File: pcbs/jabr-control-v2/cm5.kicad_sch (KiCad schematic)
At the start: 22 parts, among them J201 JST-SH-4-Vertical, Q201 DMN21D2UFB-7B, SW201 TS20-42-25-WT-160-SMT-TR, U201 NX3DV221TKX

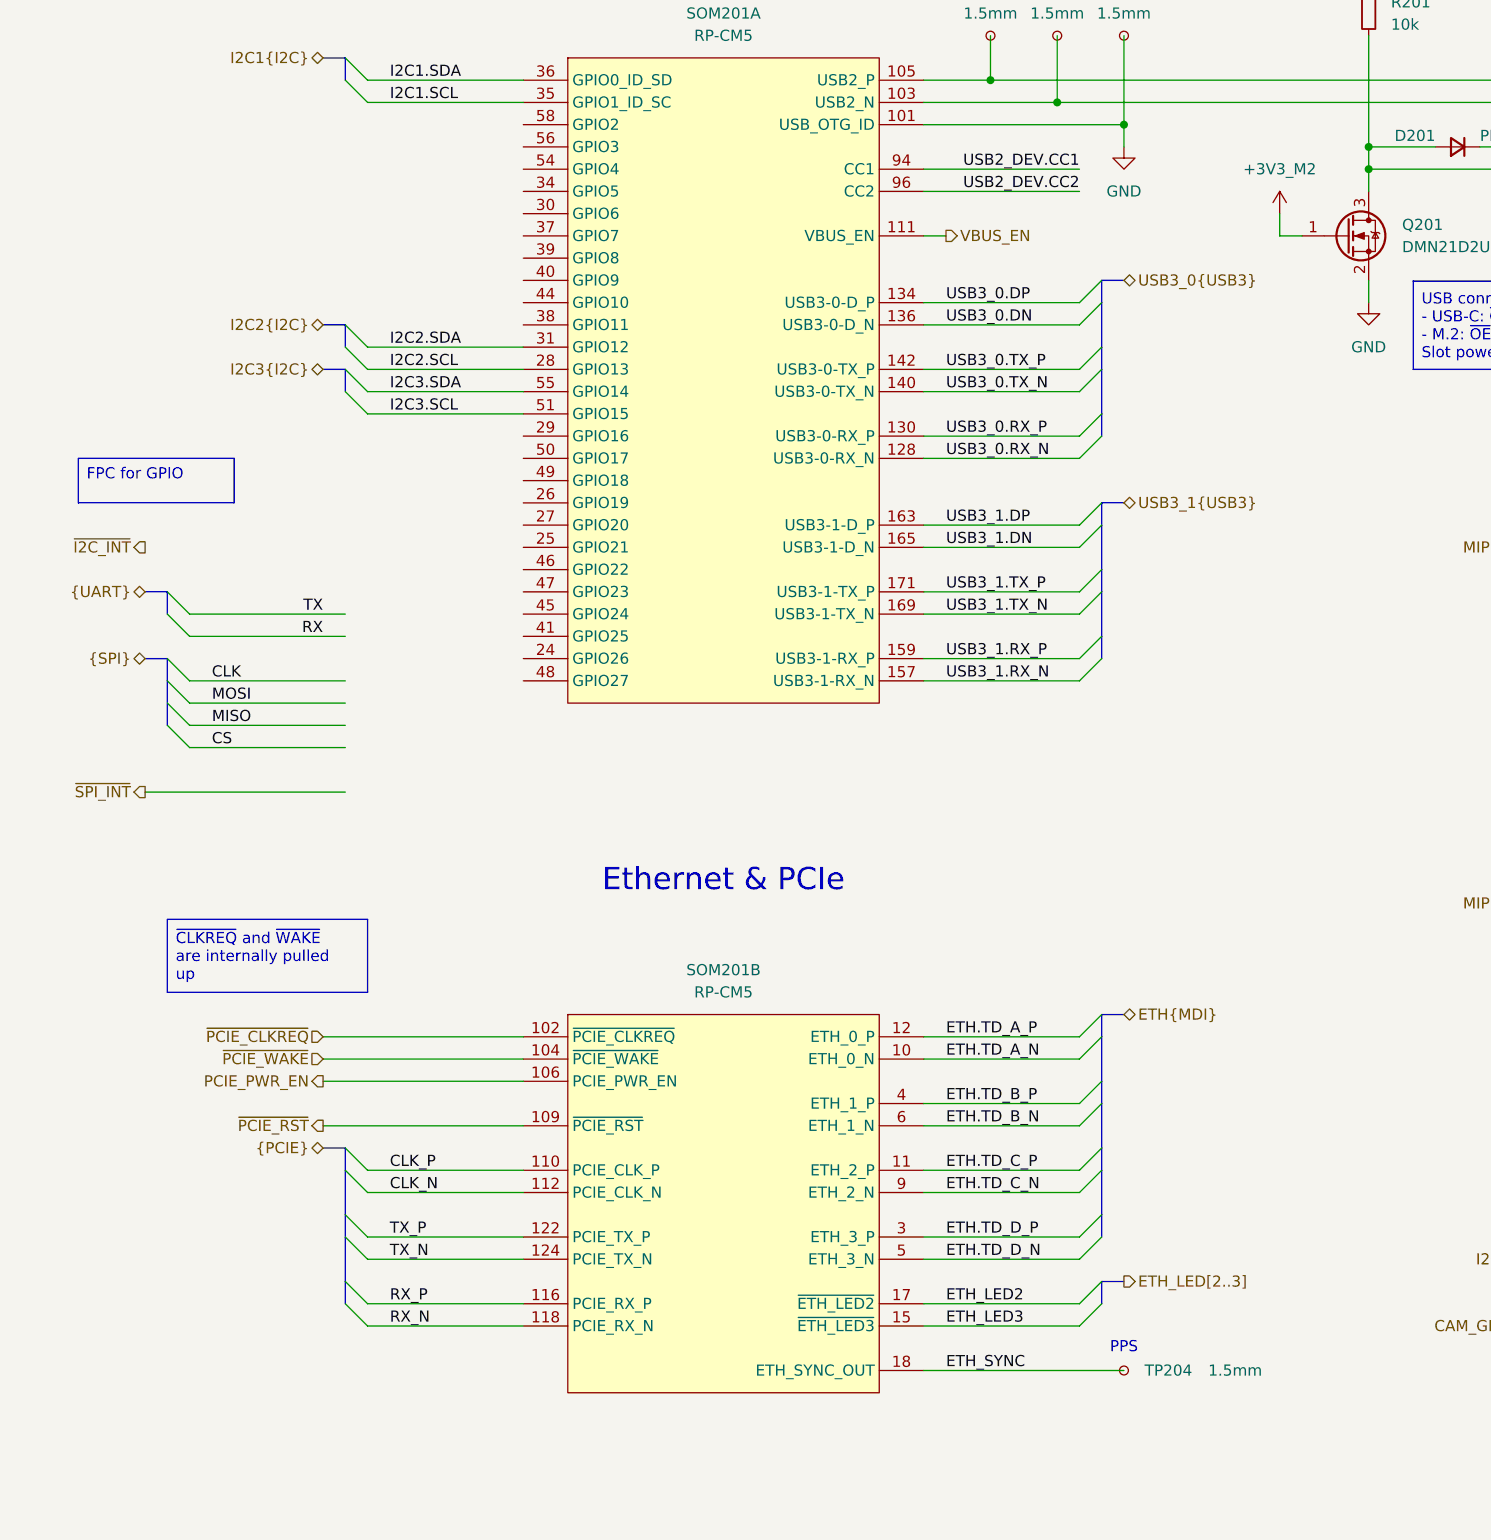
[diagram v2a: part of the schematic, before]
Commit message: PCI11010 IO done
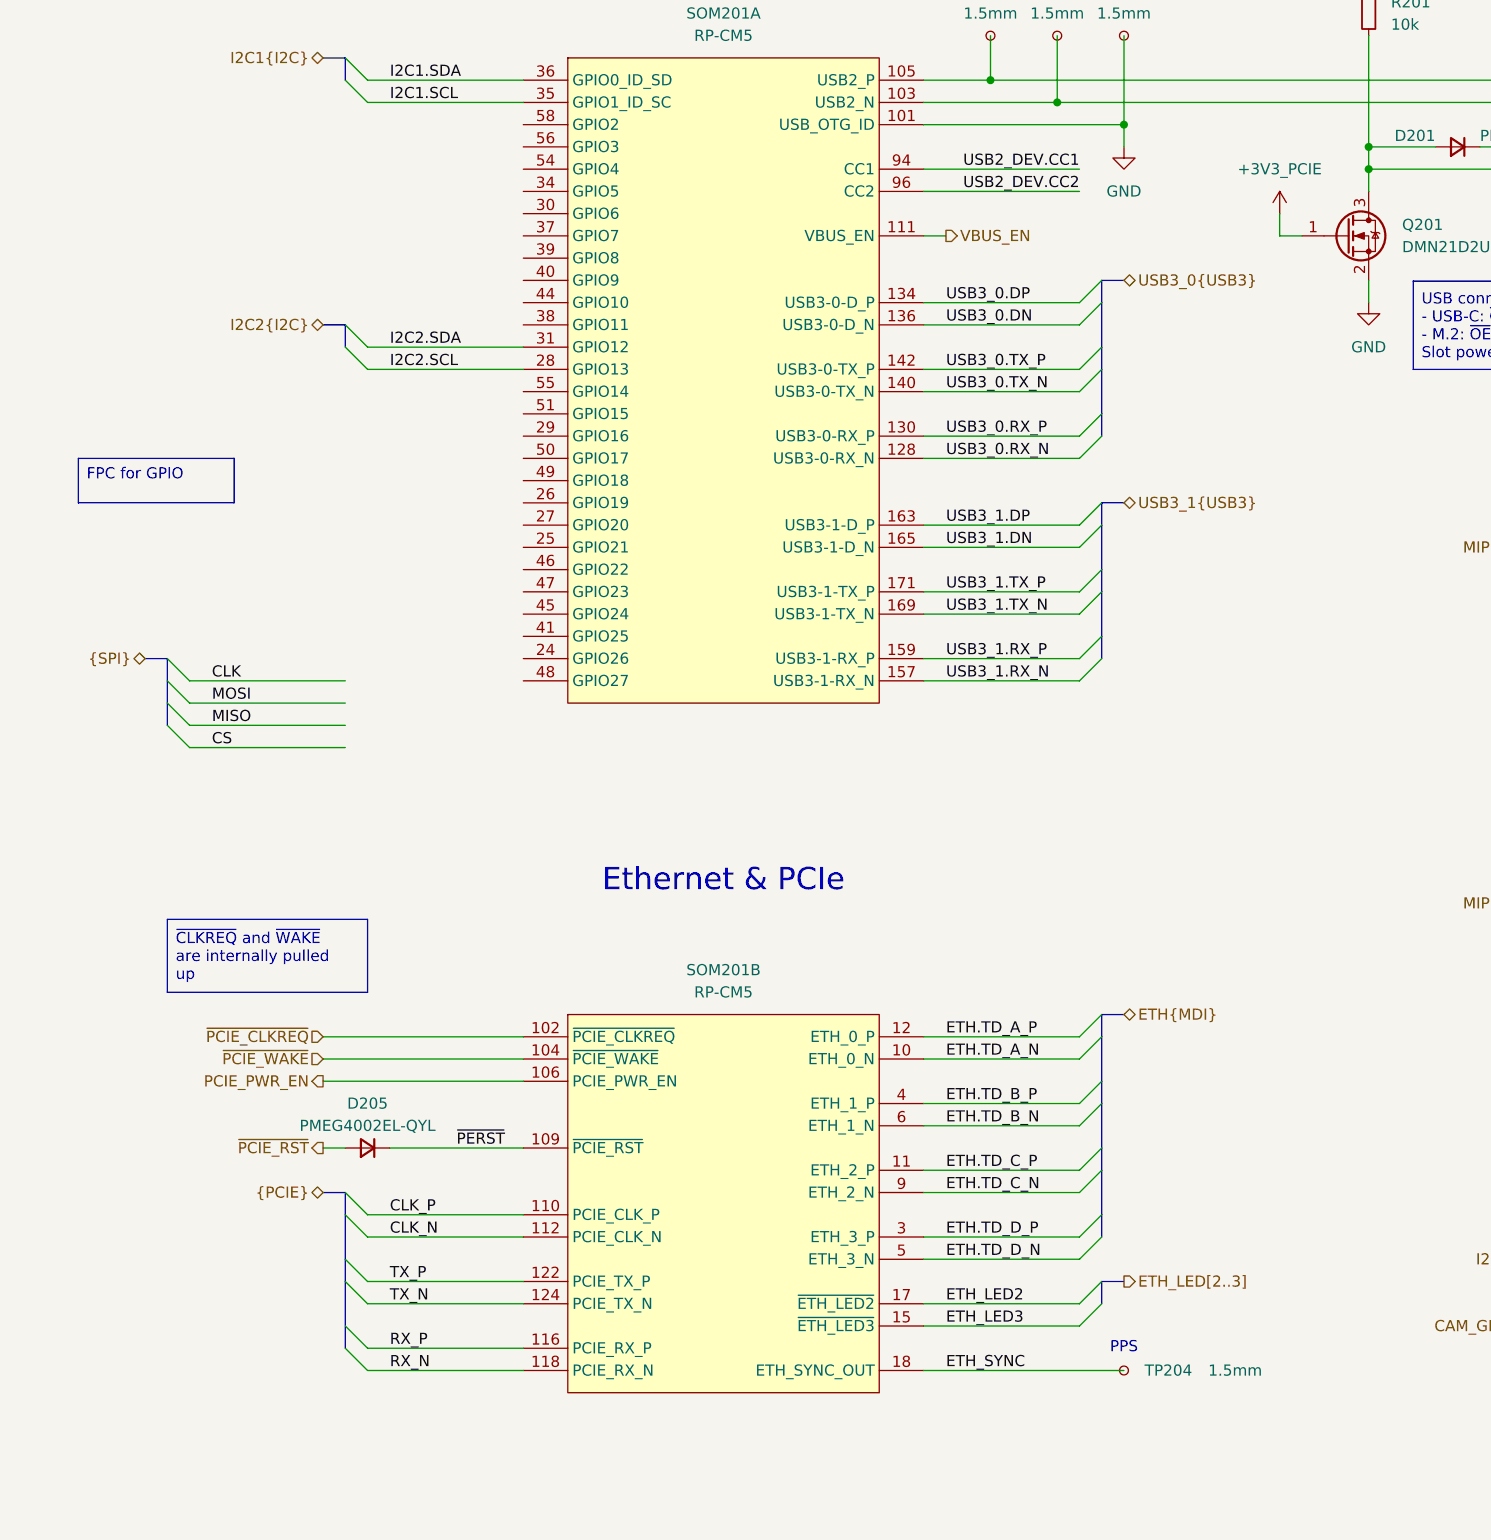
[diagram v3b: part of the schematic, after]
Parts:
- added D205: PMEG4002EL-QYL, project_footprints:PMEG4002EL-QYL, symbol DIODE:PMEG4002EL-QYL
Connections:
- net ~{PCIE_RST}: now also D205.2 (A); no longer SOM201.109 (~{PCIE_RST})
- net +3V3_M2 renamed +3V3_PCIE
- net I2C3.SCL: no longer names the net of SOM201.51 (GPIO15)
- net I2C3.SDA: no longer names the net of SOM201.55 (GPIO14)
- new net ~{PERST}: D205.1 (K), SOM201.109 (~{PCIE_RST})

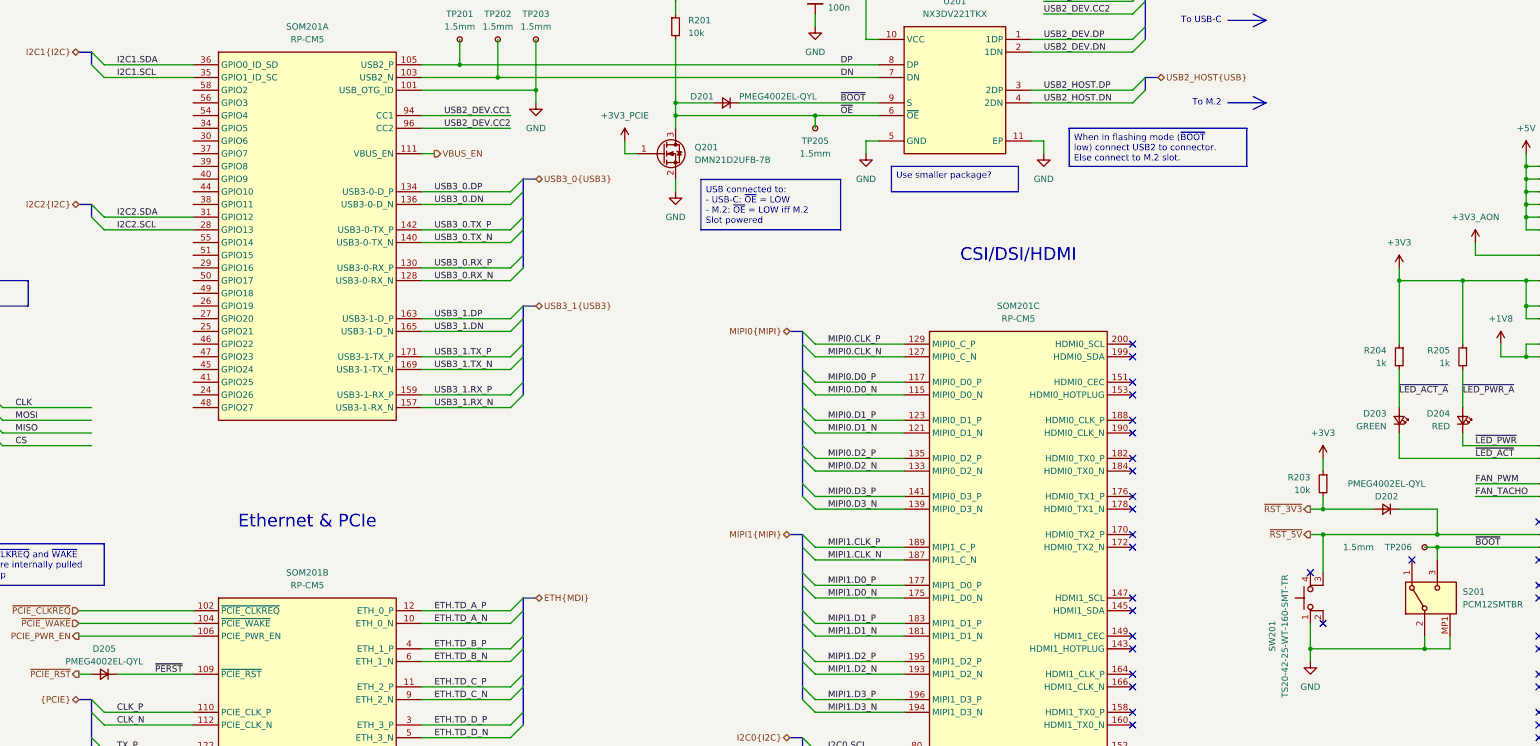
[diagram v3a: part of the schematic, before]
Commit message: Removed power button reset to switch (power will be cycled anyway)
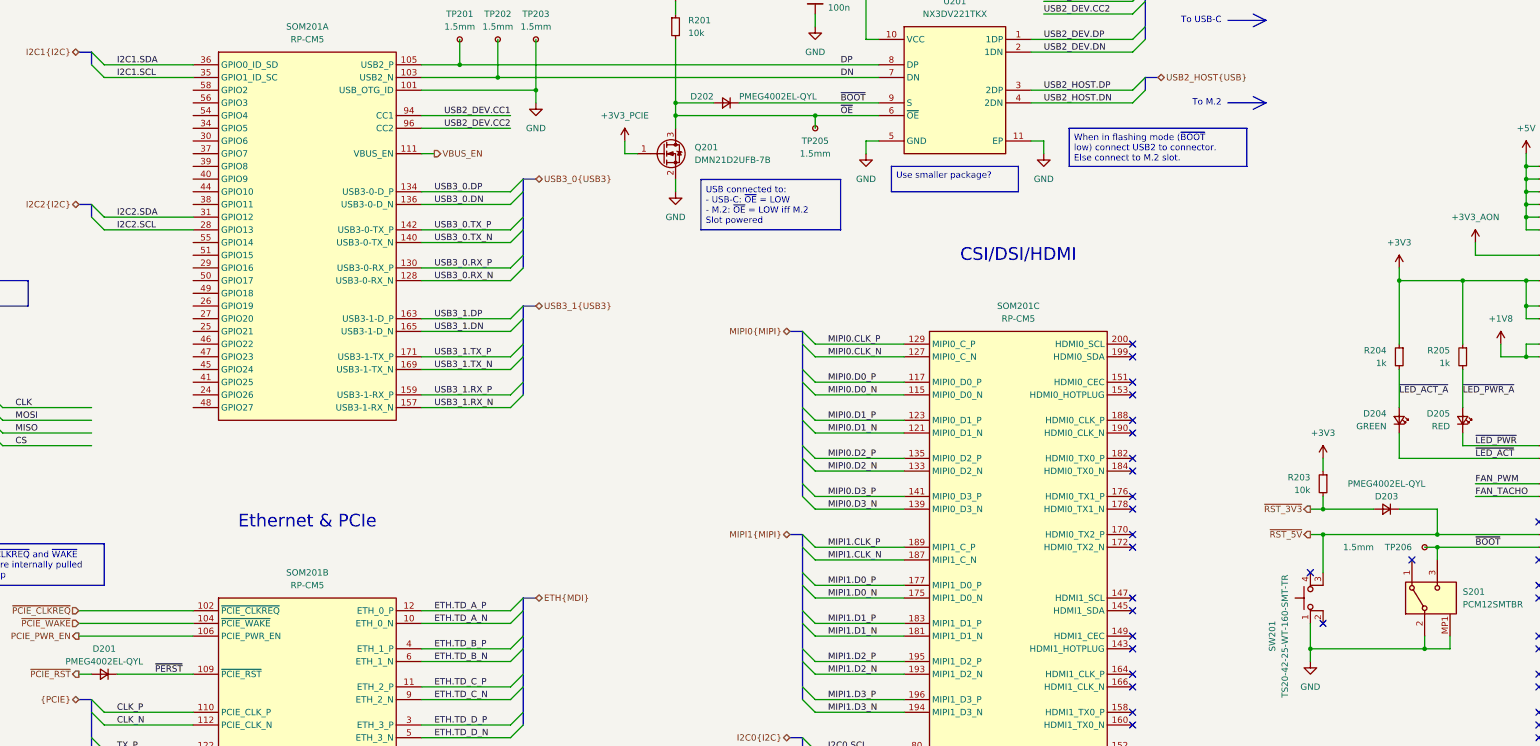
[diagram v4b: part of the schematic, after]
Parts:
- renumbered D205 to D201, D201 to D202, D202 to D203, D203 to D204, D204 to D205
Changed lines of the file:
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@@
 		(in_pos_files yes)
 		(dnp no)
-		(property "Reference" "D203"
+		(property "Reference" "D204"
 			(at 307.34 133.2864 90)
 			(show_name no)
@@
 			(project "jabr-control-v2"
 				(path "/f91ec272-d09a-4038-bbbb-962739a92c51/6befb881-6ab4-49eb-a195-35f4f02473c7"
-					(reference "D203")
+					(reference "D204")
 					(unit 1)
 				)
@@
 		(dnp no)
 		(fields_autoplaced yes)
-		(property "Reference" "#PWR0219"
+		(property "Reference" "#PWR0202"
 			(at 154.94 82.55 0)
 			(hide yes)
@@
 			(project "jabr-control-v2"
 				(path "/f91ec272-d09a-4038-bbbb-962739a92c51/6befb881-6ab4-49eb-a195-35f4f02473c7"
-					(reference "#PWR0219")
+					(reference "#PWR0202")
 					(unit 1)
 				)
@@
 		(in_pos_files yes)
 		(dnp no)
-		(property "Reference" "D204"
+		(property "Reference" "D205"
 			(at 320.04 133.2864 90)
 			(show_name no)
@@
 			(project "jabr-control-v2"
 				(path "/f91ec272-d09a-4038-bbbb-962739a92c51/6befb881-6ab4-49eb-a195-35f4f02473c7"
-					(reference "D204")
+					(reference "D205")
 					(unit 1)
 				)
@@
 		(in_pos_files yes)
 		(dnp no)
-		(property "Reference" "D202"
+		(property "Reference" "D203"
 			(at 307.34 149.86 0)
 			(show_name no)
@@
 			(project "jabr-control-v2"
 				(path "/f91ec272-d09a-4038-bbbb-962739a92c51/6befb881-6ab4-49eb-a195-35f4f02473c7"
-					(reference "D202")
+					(reference "D203")
 					(unit 1)
 				)
@@
 		(in_pos_files yes)
 		(dnp no)
-		(property "Reference" "D201"
+		(property "Reference" "D202"
 			(at 172.72 69.85 0)
 			(show_name no)
@@
 			(project "jabr-control-v2"
 				(path "/f91ec272-d09a-4038-bbbb-962739a92c51/6befb881-6ab4-49eb-a195-35f4f02473c7"
-					(reference "D201")
+					(reference "D202")
 					(unit 1)
 				)
@@
 		(in_pos_files yes)
 		(dnp no)
-		(property "Reference" "D205"
+		(property "Reference" "D201"
 			(at 50.8 180.34 0)
 			(show_name no)
@@
 			(project "jabr-control-v2"
 				(path "/f91ec272-d09a-4038-bbbb-962739a92c51/6befb881-6ab4-49eb-a195-35f4f02473c7"
-					(reference "D205")
+					(reference "D201")
 					(unit 1)
 				)

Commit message: Schematic done
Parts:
- removed D203: PMEG4002EL-QYL, project_footprints:PMEG4002EL-QYL, symbol DIODE:PMEG4002EL-QYL
- removed R203: 10k, project_footprints:R_0402, symbol DEV:R_SMALL
- removed TP204: 1.5mm, project_footprints:TestPoint_Pad_D1.5mm, symbol Connector:TestPoint_Small
- added D701: PMEG4002EL-QYL, project_footprints:PMEG4002EL-QYL, symbol DIODE:PMEG4002EL-QYL
- added J701: FFC3A20-05-G, project_footprints:FFC3A2005G, symbol CONN-FPC:FFC3A20-05-G
- added TP701, TP704, TP707: 1.5mm, project_footprints:TestPoint_Pad_D1.5mm, symbol Connector:TestPoint_Small
- added U701: PESD4USB3BTTS-QX, project_footprints:PESD4USB3BTTSQX, symbol TVS:PESD4USB3BTTS-QX
- C701: renamed from C201; footprint (none) -> project_footprints:C_0402
- D704: renamed from D204; footprint (none) -> project_footprints:LED_0402
- D705: renamed from D205; footprint (none) -> project_footprints:LED_0402
- SW701: renamed from SW201; footprint TS204225WT160SMTTR -> project_footprints:TS204225WT160SMTTR
- U702: renamed from U201; value NX3DV221TKX -> NX3DV221GM; footprint project_footprints:SON50P300X300X100-11N -> project_footprints:NX3DV221GM115; symbol COMM-MUX:NX3DV221TKX -> COMM-MUX:NX3DV221GM; Height 1 -> 0.5
- renumbered D201 to D702, D202 to D703, J201 to J702, Q201 to Q701, R201 to R701, R202 to R702, R204 to R703, R205 to R704, S201 to S701, SOM201 to SOM701, TP201 to TP702, TP202 to TP703, TP203 to TP705, TP205 to TP706, TP206 to TP708
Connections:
- net +5V: now also J701.1
- net GND: now also J701.5, U701.3 (GND_1), U701.8 (GND_2)
- net RX: now reaches SOM701.34 (GPIO5)
- net RX: now also J701.4, U701.1 (CH1), U701.10 (NC)
- net GPIO27: now reaches SOM701.48 (GPIO27)
- net GPIO27: now also TP701.1
- net TX: now reaches SOM701.54 (GPIO4)
- net TX: now also J701.3, U701.2 (CH2), U701.9 (NC)
- net NRST: now reaches SOM701.56 (GPIO3)
- net NRST: now also D701.1 (K)
- net ETH_SYNC renamed ETH_SYNC_OUT
- net ETH_SYNC_OUT: now also TP704.1
- net I2C0.SCL renamed MIPI0.SCL
- net I2C0.SDA renamed MIPI0.SDA
- net I2C1.SCL renamed MIPI1.SCL
- net I2C1.SDA renamed MIPI1.SDA
- net ~{RST_5V} renamed PWR_BUT
- net PWR_BUT: now also TP707.1
- new net: U701.5 (CH4), U701.6 (NC)
- new net NRST_CONN: D701.2 (A), J701.2, U701.4 (CH3), U701.7 (NC)
- no-connect marks 45 -> 66
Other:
- note added: "PPS_CM5"
- note added: "PPS_SPE"
- note removed: "PPS"
- moved on the sheet: C701, D702, D703, D704, D705, J702, Q701, R701, R702, R703, R704, S701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
